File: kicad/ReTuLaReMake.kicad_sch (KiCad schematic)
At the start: 23 parts, among them J1 40 Pin DIP Header, U1 ATF1508AS-10AU100

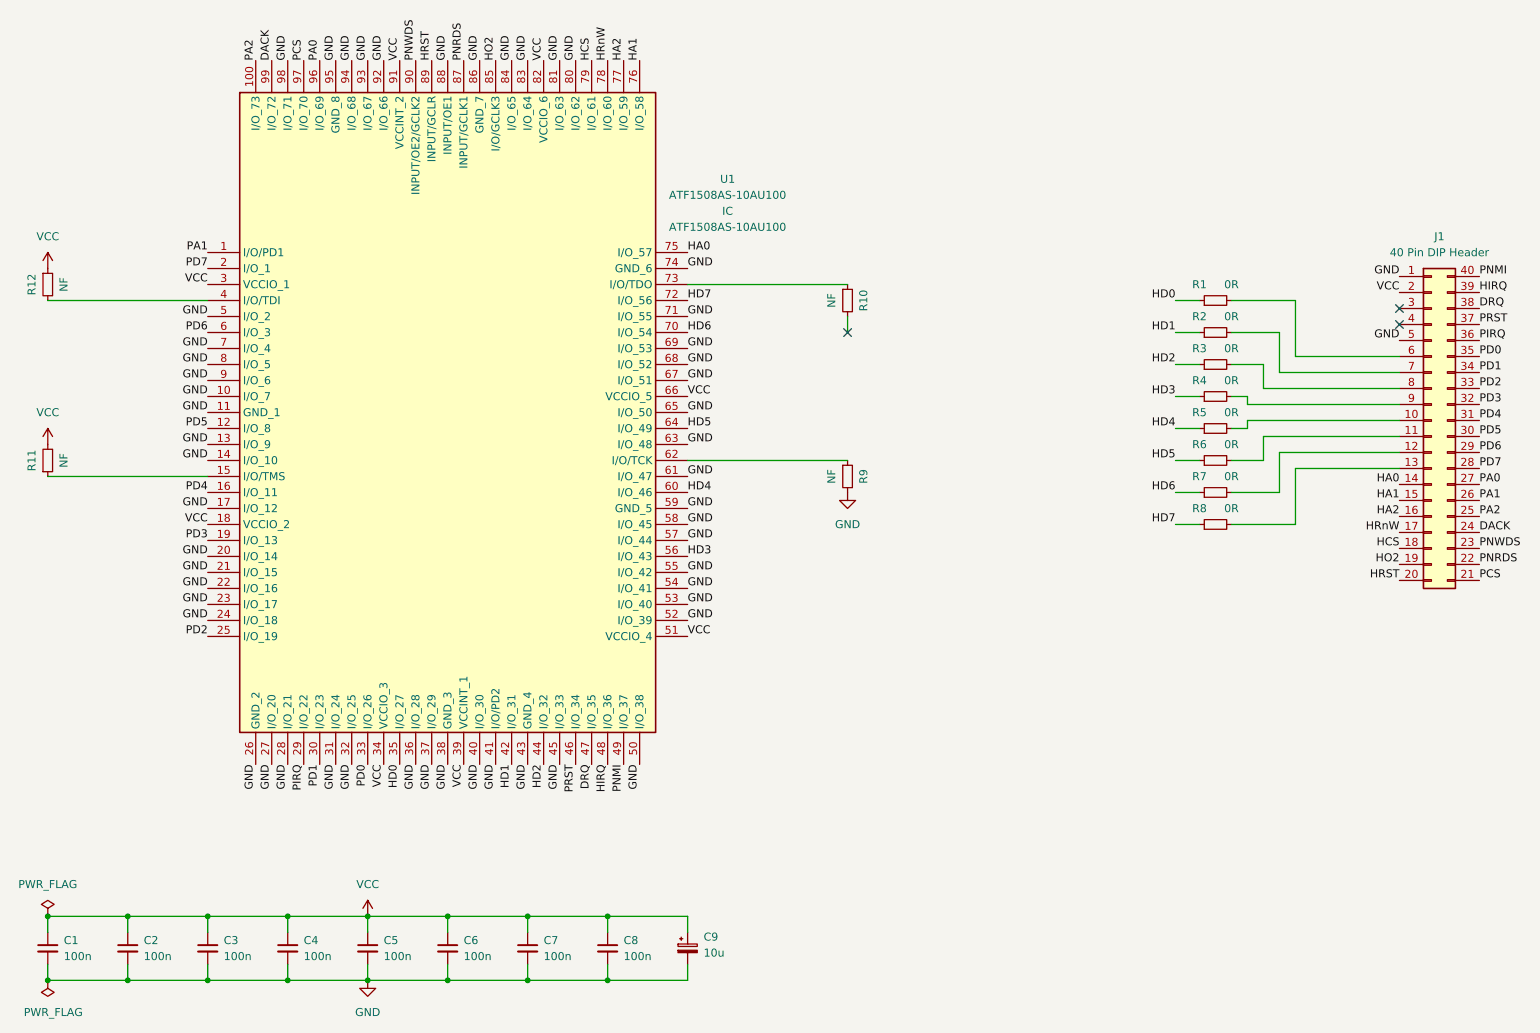
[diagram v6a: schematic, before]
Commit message: KiCAD: Added JTAG Connector
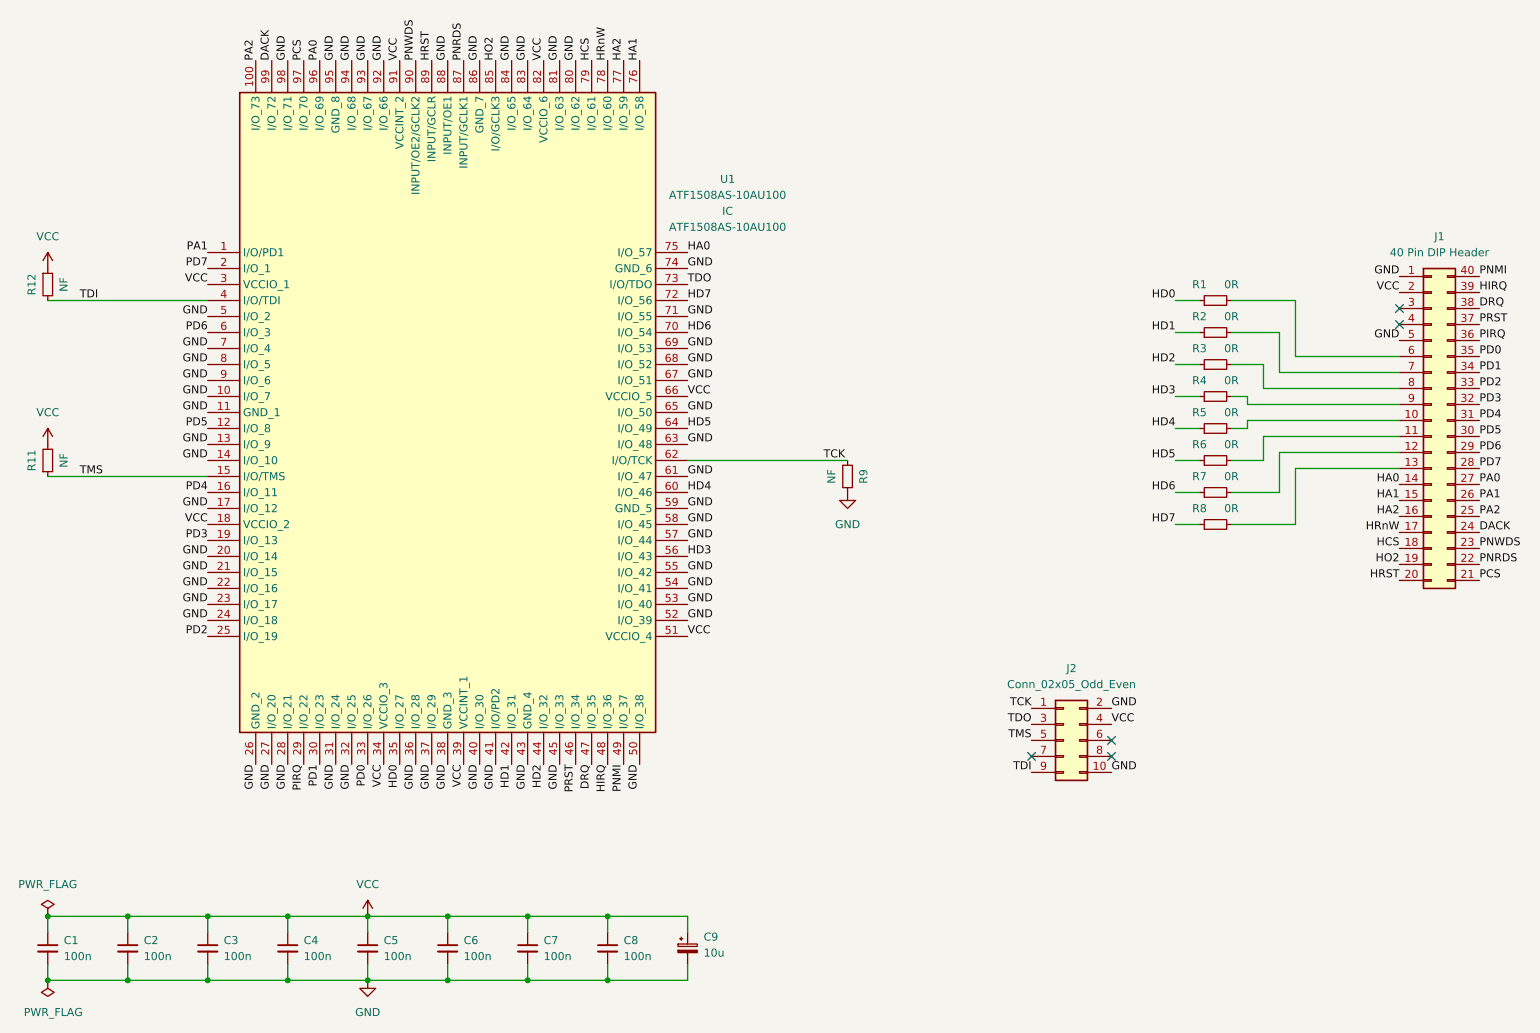
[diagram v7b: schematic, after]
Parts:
- removed R10: NF, Resistor_SMD:R_1206_3216Metric, symbol Device:R_Small
- added J2: Conn_02x05_Odd_Even, Connector_PinHeader_2.54mm:PinHeader_2x05_P2.54mm_Vertical, symbol Connector_Generic:Conn_02x05_Odd_Even
- R11, R12, R9: footprint Resistor_SMD:R_1206_3216Metric -> Resistor_SMD:R_0805_2012Metric_Pad1.20x1.40mm_HandSolder
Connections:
- net GND: now also J2.10 (Pin_10), J2.2 (Pin_2)
- net VCC: now also J2.4 (Pin_4)
- net TDO: now reaches U1.73 (I/O/TDO)
- net TDO: now also J2.3 (Pin_3)
- net TMS: now reaches R11.1, U1.15 (I/O/TMS)
- net TMS: now also J2.5 (Pin_5)
- net TDI: now reaches R12.2, U1.4 (I/O/TDI)
- net TDI: now also J2.9 (Pin_9)
- net TCK: now reaches R9.1, U1.62 (I/O/TCK)
- net TCK: now also J2.1 (Pin_1)
- no-connect marks 3 -> 5
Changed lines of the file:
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@@
   )
   (no_connect (at 255.27 80.01))
+  (no_connect (at 209.55 148.59))
   (no_connect (at 255.27 77.47))
-  (no_connect (at 167.64 81.28))
+  (no_connect (at 196.85 148.59))
+  (no_connect (at 209.55 146.05))
   (wire (pts (xy 255.27 97.79) (xy 233.68 97.79))
     (stroke (width 0) (type default) (color 0 0 0 0))
@@
     (stroke (width 0) (type default) (color 0 0 0 0))
   )
-  (wire (pts (xy 142.24 73.66) (xy 167.64 73.66))
-    (stroke (width 0) (type default) (color 0 0 0 0))
-  )
   (wire (pts (xy 238.76 85.09) (xy 238.76 76.2))
     (stroke (width 0) (type default) (color 0 0 0 0))
@@
     (stroke (width 0) (type default) (color 0 0 0 0))
   )
-  (wire (pts (xy 167.64 81.28) (xy 167.64 78.74))
-    (stroke (width 0) (type default) (color 0 0 0 0))
-  )
   (wire (pts (xy 255.27 102.87) (xy 238.76 102.87))
     (stroke (width 0) (type default) (color 0 0 0 0))
@@
     (effects (font (size 1.27 1.27)) (justify right bottom))
   )
+  (label "GND" (at 209.55 151.13 0)
+    (effects (font (size 1.27 1.27)) (justify left bottom))
+  )
   (label "HD2" (at 219.71 86.36 180)
     (effects (font (size 1.27 1.27)) (justify right bottom))
@@
     (effects (font (size 1.27 1.27)) (justify left bottom))
   )
+  (label "TDO" (at 142.24 73.66 0)
+    (effects (font (size 1.27 1.27)) (justify left bottom))
+  )
   (label "GND" (at 66.04 127 180)
     (effects (font (size 1.27 1.27)) (justify right bottom))
@@
     (effects (font (size 1.27 1.27)) (justify left bottom))
   )
+  (label "TCK" (at 196.85 140.97 180)
+    (effects (font (size 1.27 1.27)) (justify right bottom))
+  )
   (label "VCC" (at 106.68 149.86 270)
     (effects (font (size 1.27 1.27)) (justify right bottom))
@@
     (effects (font (size 1.27 1.27)) (justify right bottom))
   )
+  (label "TCK" (at 163.83 101.6 0)
+    (effects (font (size 1.27 1.27)) (justify left bottom))
+  )
   (label "PA0" (at 267.97 105.41 0)
     (effects (font (size 1.27 1.27)) (justify left bottom))
@@
     (effects (font (size 1.27 1.27)) (justify right bottom))
   )
+  (label "TMS" (at 196.85 146.05 180)
+    (effects (font (size 1.27 1.27)) (justify right bottom))
+  )
   (label "GND" (at 104.14 149.86 270)
     (effects (font (size 1.27 1.27)) (justify right bottom))
   )
+  (label "TDI" (at 196.85 151.13 180)
+    (effects (font (size 1.27 1.27)) (justify right bottom))
+  )
   (label "PNWDS" (at 99.06 38.1 90)
     (effects (font (size 1.27 1.27)) (justify left bottom))
@@
     (effects (font (size 1.27 1.27)) (justify right bottom))
   )
+  (label "TDI" (at 45.72 76.2 0)
+    (effects (font (size 1.27 1.27)) (justify left bottom))
+  )
   (label "VCC" (at 96.52 38.1 90)
     (effects (font (size 1.27 1.27)) (justify left bottom))
@@
     (effects (font (size 1.27 1.27)) (justify right bottom))
   )
+  (label "GND" (at 209.55 140.97 0)
+    (effects (font (size 1.27 1.27)) (justify left bottom))
+  )
   (label "GND" (at 116.84 149.86 270)
     (effects (font (size 1.27 1.27)) (justify right bottom))
@@
     (effects (font (size 1.27 1.27)) (justify right bottom))
   )
+  (label "TDO" (at 196.85 143.51 180)
+    (effects (font (size 1.27 1.27)) (justify right bottom))
+  )
   (label "GND" (at 86.36 38.1 90)
     (effects (font (size 1.27 1.27)) (justify left bottom))
@@
     (effects (font (size 1.27 1.27)) (justify left bottom))
   )
+  (label "TMS" (at 45.72 104.14 0)
+    (effects (font (size 1.27 1.27)) (justify left bottom))
+  )
   (label "HCS" (at 255.27 115.57 180)
     (effects (font (size 1.27 1.27)) (justify right bottom))
@@
     (effects (font (size 1.27 1.27)) (justify right bottom))
   )
+  (label "VCC" (at 209.55 143.51 0)
+    (effects (font (size 1.27 1.27)) (justify left bottom))
+  )
   (label "HRST" (at 255.27 120.65 180)
     (effects (font (size 1.27 1.27)) (justify right bottom))
@@
   (label "GND" (at 109.22 149.86 270)
     (effects (font (size 1.27 1.27)) (justify right bottom))
-  )
-  (symbol (lib_id "Device:R_Small") (at 167.64 76.2 0) (unit 1)
-    (in_bom yes) (on_board yes)
-    (property "Reference" "R10" (id 0) (at 170.18 76.2 90))
-    (property "Value" "NF" (id 1) (at 165.1 76.2 90))
-    (property "Footprint" "Resistor_SMD:R_1206_3216Metric" (id 2) (at 167.64 76.2 0)
-      (effects (font (size 1.27 1.27)) hide)
-    )
-    (property "Datasheet" "~" (id 3) (at 167.64 76.2 0)
-      (effects (font (size 1.27 1.27)) hide)
-    )
-    (pin "1")
-    (pin "2")
   )
   (symbol (lib_id "Device:C_Small") (at 116.84 179.07 0) (unit 1)
@@
     (property "Reference" "R12" (id 0) (at 38.1 73.66 90))
     (property "Value" "NF" (id 1) (at 43.18 73.66 90))
-    (property "Footprint" "Resistor_SMD:R_1206_3216Metric" (id 2) (at 40.64 73.66 0)
+    (property "Footprint" "Resistor_SMD:R_0805_2012Metric_Pad1.20x1.40mm_HandSolder" (id 2) (at 40.64 73.66 0)
       (effects (font (size 1.27 1.27)) hide)
     )
@@
     (pin "1")
     (pin "2")
+  )
+  (symbol (lib_id "Connector_Generic:Conn_02x05_Odd_Even") (at 201.93 146.05 0) (unit 1)
+    (in_bom yes) (on_board yes) (fields_autoplaced)
+    (property "Reference" "J2" (id 0) (at 203.2 134.62 0))
+    (property "Value" "Conn_02x05_Odd_Even" (id 1) (at 203.2 137.16 0))
+    (property "Footprint" "Connector_PinHeader_2.54mm:PinHeader_2x05_P2.54mm_Vertical" (id 2) (at 201.93 146.05 0)
+      (effects (font (size 1.27 1.27)) hide)
+    )
+    (property "Datasheet" "~" (id 3) (at 201.93 146.05 0)
+      (effects (font (size 1.27 1.27)) hide)
+    )
+    (pin "1")
+    (pin "10")
+    (pin "2")
+    (pin "3")
+    (pin "4")
+    (pin "5")
+    (pin "6")
+    (pin "7")
+    (pin "8")
+    (pin "9")
   )
   (symbol (lib_id "Device:C_Small") (at 129.54 179.07 0) (unit 1)
@@
     (property "Reference" "R9" (id 0) (at 170.18 104.14 90))
     (property "Value" "NF" (id 1) (at 165.1 104.14 90))
-    (property "Footprint" "Resistor_SMD:R_1206_3216Metric" (id 2) (at 167.64 104.14 0)
+    (property "Footprint" "Resistor_SMD:R_0805_2012Metric_Pad1.20x1.40mm_HandSolder" (id 2) (at 167.64 104.14 0)
       (effects (font (size 1.27 1.27)) hide)
     )
@@
     (property "Reference" "R11" (id 0) (at 38.1 101.6 90))
     (property "Value" "NF" (id 1) (at 43.18 101.6 90))
-    (property "Footprint" "Resistor_SMD:R_1206_3216Metric" (id 2) (at 40.64 101.6 0)
+    (property "Footprint" "Resistor_SMD:R_0805_2012Metric_Pad1.20x1.40mm_HandSolder" (id 2) (at 40.64 101.6 0)
       (effects (font (size 1.27 1.27)) hide)
     )
@@
       (reference "J1") (unit 1) (value "40 Pin DIP Header") (footprint "myfootprints:DIP-40_W15.24mm_Header")
     )
+    (path "/72801af5-6ff2-4007-94eb-b30fe5d8e3a7"
+      (reference "J2") (unit 1) (value "Conn_02x05_Odd_Even") (footprint "Connector_PinHeader_2.54mm:PinHeader_2x05_P2.54mm_Vertical")
+    )
     (path "/964de713-4bf4-4d62-9515-7459808eb087"
       (reference "R1") (unit 1) (value "0R") (footprint "Resistor_SMD:R_0805_2012Metric_Pad1.20x1.40mm_HandSolder")
@@
     )
     (path "/99dba31c-ee68-4162-a785-0f0e83785d19"
-      (reference "R9") (unit 1) (value "NF") (footprint "Resistor_SMD:R_1206_3216Metric")
-    )
-    (path "/1b8eeb4c-aac9-4ce0-a1ca-621ae0ba9958"
-      (reference "R10") (unit 1) (value "NF") (footprint "Resistor_SMD:R_1206_3216Metric")
+      (reference "R9") (unit 1) (value "NF") (footprint "Resistor_SMD:R_0805_2012Metric_Pad1.20x1.40mm_HandSolder")
     )
     (path "/9c96dc6c-4b7f-4fc1-b6f4-7cfb4c94001c"
-      (reference "R11") (unit 1) (value "NF") (footprint "Resistor_SMD:R_1206_3216Metric")
+      (reference "R11") (unit 1) (value "NF") (footprint "Resistor_SMD:R_0805_2012Metric_Pad1.20x1.40mm_HandSolder")
     )
     (path "/6df6e71d-43b0-4d40-beec-529e26c51d4b"
-      (reference "R12") (unit 1) (value "NF") (footprint "Resistor_SMD:R_1206_3216Metric")
+      (reference "R12") (unit 1) (value "NF") (footprint "Resistor_SMD:R_0805_2012Metric_Pad1.20x1.40mm_HandSolder")
     )
     (path "/5667c8b7-51f0-4e01-9182-7dd1424c90df"

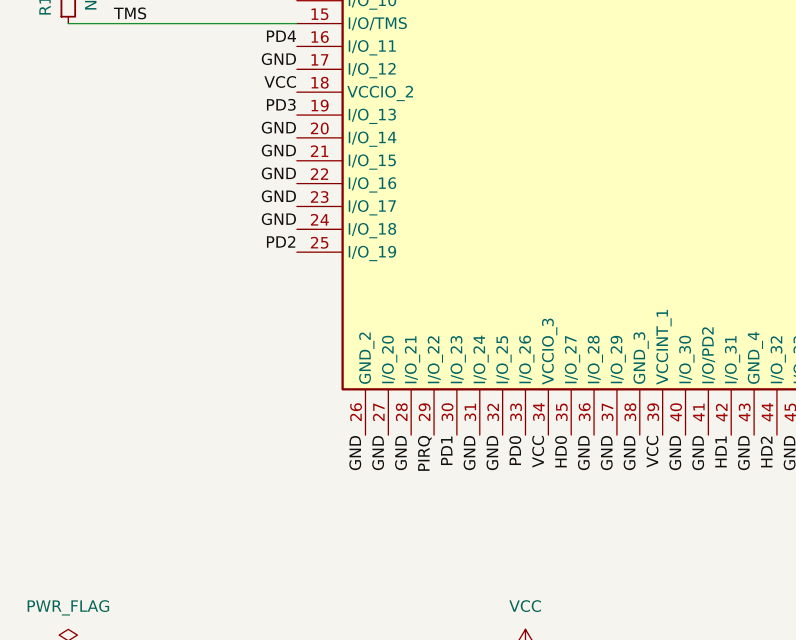
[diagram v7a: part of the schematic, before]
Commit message: KiCAD: Update pins for p_data2/1/0
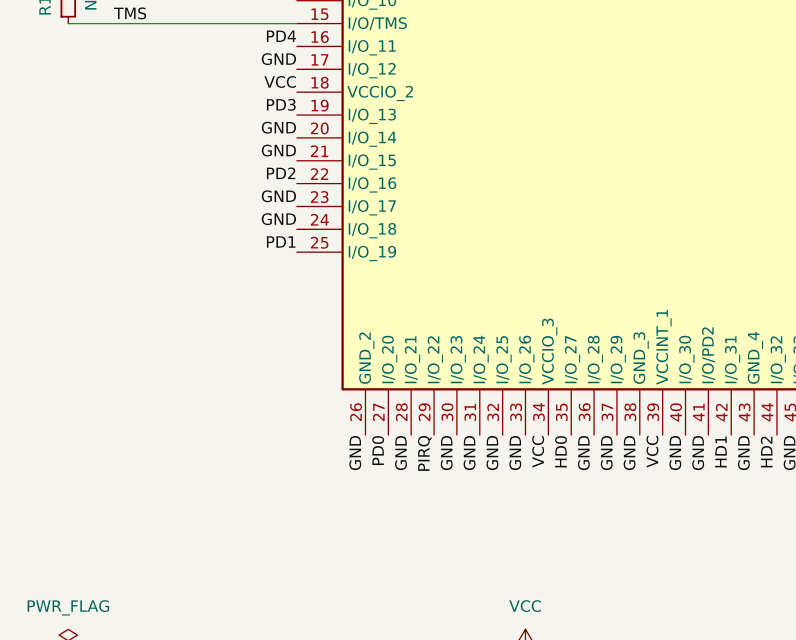
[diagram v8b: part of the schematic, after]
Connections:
- net GND: now also U1.30 (I/O_23), U1.33 (I/O_26); no longer U1.22 (I/O_16), U1.27 (I/O_20)
- net PD0: now also U1.27 (I/O_20); no longer U1.33 (I/O_26)
- net PD1: now also U1.25 (I/O_19); no longer U1.30 (I/O_23)
- net PD2: now also U1.22 (I/O_16); no longer U1.25 (I/O_19)
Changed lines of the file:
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@@
     (effects (font (size 1.27 1.27)) (justify left bottom))
   )
-  (label "GND" (at 66.04 121.92 180)
+  (label "GND" (at 83.82 149.86 270)
     (effects (font (size 1.27 1.27)) (justify right bottom))
   )
@@
     (effects (font (size 1.27 1.27)) (justify left bottom))
   )
-  (label "GND" (at 76.2 149.86 270)
+  (label "GND" (at 91.44 149.86 270)
     (effects (font (size 1.27 1.27)) (justify right bottom))
   )
@@
     (effects (font (size 1.27 1.27)) (justify left bottom))
   )
-  (label "PD2" (at 66.04 129.54 180)
+  (label "PD2" (at 66.04 121.92 180)
     (effects (font (size 1.27 1.27)) (justify right bottom))
   )
@@
     (effects (font (size 1.27 1.27)) (justify left bottom))
   )
-  (label "PD0" (at 91.44 149.86 270)
+  (label "PD0" (at 76.2 149.86 270)
     (effects (font (size 1.27 1.27)) (justify right bottom))
   )
@@
     (effects (font (size 1.27 1.27)) (justify left bottom))
   )
-  (label "PD1" (at 83.82 149.86 270)
-    (effects (font (size 1.27 1.27)) (justify right bottom))
-  )
+  (label "PD1" (at 66.04 129.54 180)
+    (effects (font (size 1.27 1.27)) (justify right bottom))
+  )
